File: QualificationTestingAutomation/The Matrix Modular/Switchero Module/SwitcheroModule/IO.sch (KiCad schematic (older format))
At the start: 8 parts, among them J1 Conn_02x32_Counter_Clockwise_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, J2 OBD Connector, J3 OBD Connector, J6 Conn_02x32_Counter_Clockwise_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

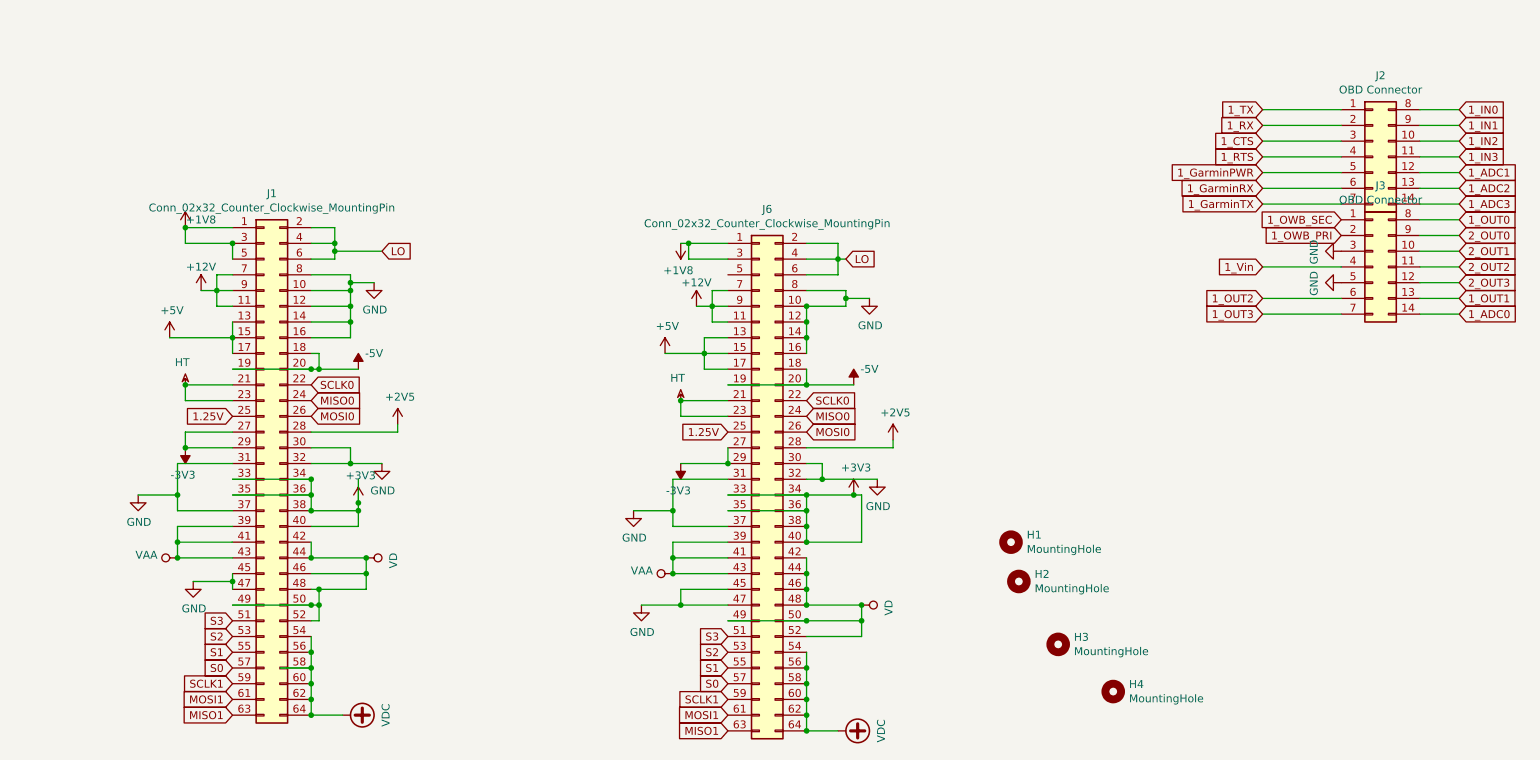
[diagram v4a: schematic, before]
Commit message: IO clean up added the 1v25 reference to Matrix Changed Some of the labels to more legible names.
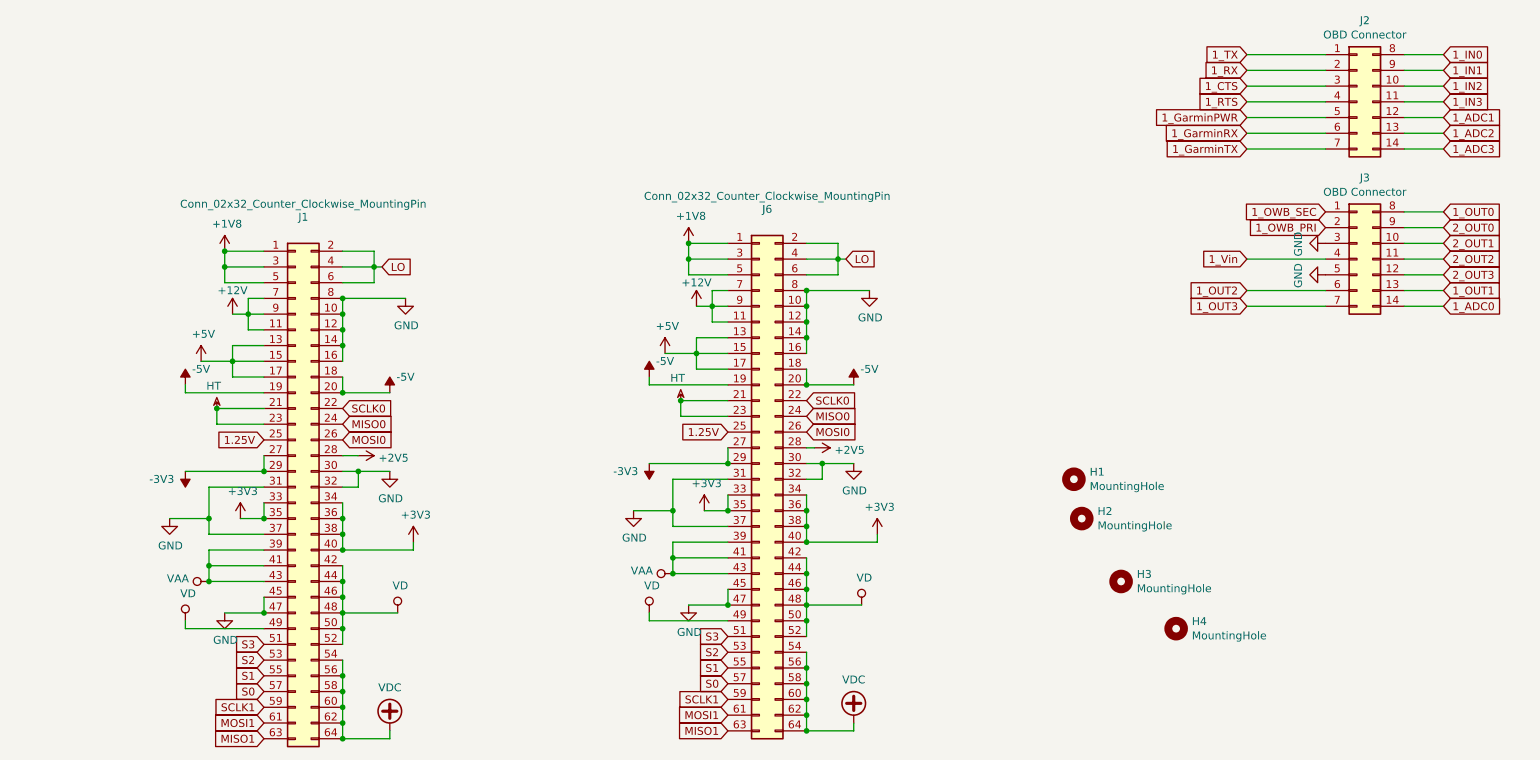
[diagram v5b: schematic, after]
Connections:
- net +1V8: now also J6.5 (Pin_5)
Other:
- moved on the sheet: H2, H3, H4, J2, J3

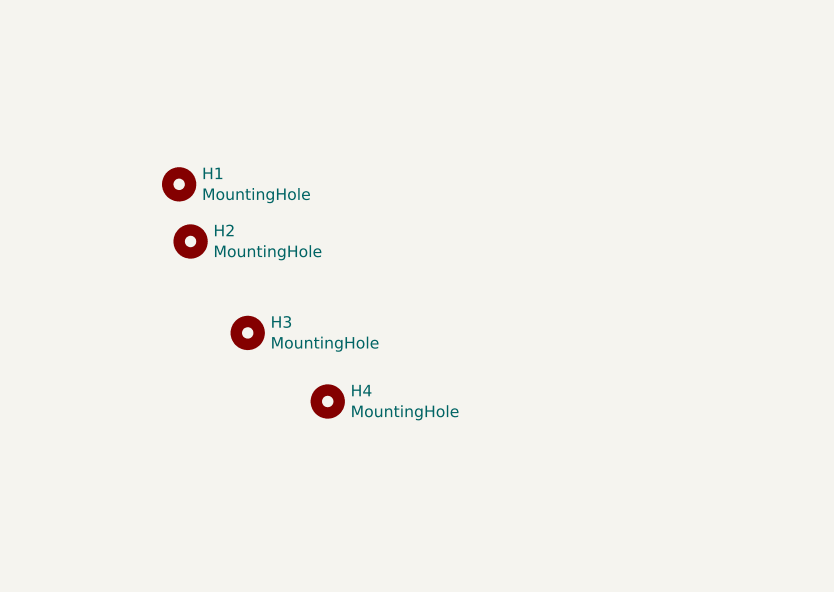
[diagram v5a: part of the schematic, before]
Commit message: Reefero Module PCB design
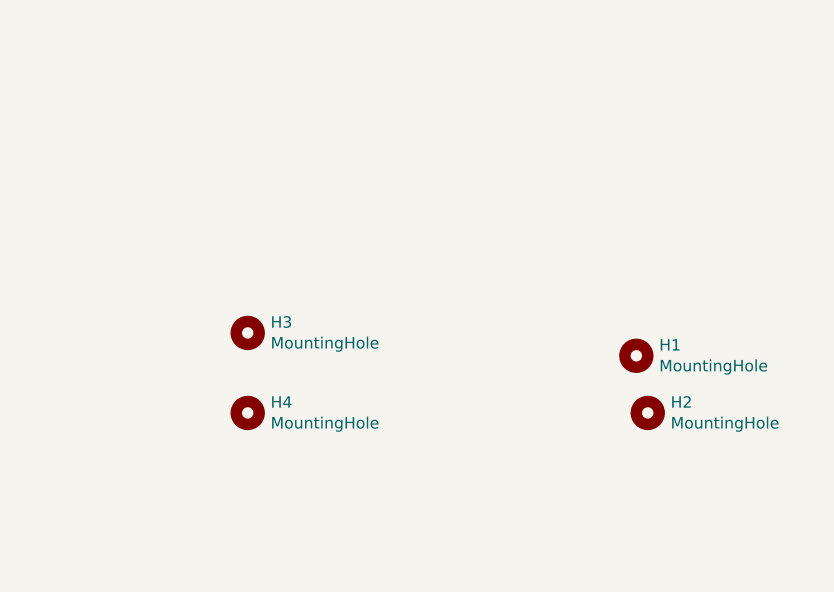
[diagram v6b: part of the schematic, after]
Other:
- moved on the sheet: H1, H2, H4
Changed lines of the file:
@@
 L Mechanical:MountingHole H?
 U 1 1 5CA6BACD
-P 8100 3700
+P 10100 4450
 AR Path="/5D942532/5CA6BACD" Ref="H?"  Part="1"
 AR Path="/5D968A33/5CA6BACD" Ref="H?"  Part="1"
 AR Path="/5C90F517/5CA6BACD" Ref="H1"  Part="1"
-F 0 "H1" H 8200 3746 50  0000 L CNN
-F 1 "MountingHole" H 8200 3655 50  0000 L CNN
-F 2 "MountingHole:MountingHole_2.5mm" H 8100 3700 50  0001 C CNN
-F 3 "~" H 8100 3700 50  0001 C CNN
-	1    8100 3700
+F 0 "H1" H 10200 4496 50  0000 L CNN
+F 1 "MountingHole" H 10200 4405 50  0000 L CNN
+F 2 "MountingHole:MountingHole_2.5mm" H 10100 4450 50  0001 C CNN
+F 3 "~" H 10100 4450 50  0001 C CNN
+	1    10100 4450
 	1    0    0    -1
 $EndComp
@@
 L Mechanical:MountingHole H?
 U 1 1 5E817FBB
-P 8150 3950
+P 10150 4700
 AR Path="/5D942532/5E817FBB" Ref="H?"  Part="1"
 AR Path="/5D968A33/5E817FBB" Ref="H?"  Part="1"
 AR Path="/5C90F517/5E817FBB" Ref="H2"  Part="1"
-F 0 "H2" H 8250 3996 50  0000 L CNN
-F 1 "MountingHole" H 8250 3905 50  0000 L CNN
-F 2 "MountingHole:MountingHole_2.5mm" H 8150 3950 50  0001 C CNN
-F 3 "~" H 8150 3950 50  0001 C CNN
-	1    8150 3950
+F 0 "H2" H 10250 4746 50  0000 L CNN
+F 1 "MountingHole" H 10250 4655 50  0000 L CNN
+F 2 "MountingHole:MountingHole_2.5mm" H 10150 4700 50  0001 C CNN
+F 3 "~" H 10150 4700 50  0001 C CNN
+	1    10150 4700
 	1    0    0    -1
 $EndComp
@@
 L Mechanical:MountingHole H?
 U 1 1 5E82AE9C
-P 8750 4650
+P 8400 4700
 AR Path="/5D942532/5E82AE9C" Ref="H?"  Part="1"
 AR Path="/5D968A33/5E82AE9C" Ref="H?"  Part="1"
 AR Path="/5C90F517/5E82AE9C" Ref="H4"  Part="1"
-F 0 "H4" H 8850 4696 50  0000 L CNN
-F 1 "MountingHole" H 8850 4605 50  0000 L CNN
-F 2 "MountingHole:MountingHole_2.5mm" H 8750 4650 50  0001 C CNN
-F 3 "~" H 8750 4650 50  0001 C CNN
-	1    8750 4650
+F 0 "H4" H 8500 4746 50  0000 L CNN
+F 1 "MountingHole" H 8500 4655 50  0000 L CNN
+F 2 "MountingHole:MountingHole_2.5mm" H 8400 4700 50  0001 C CNN
+F 3 "~" H 8400 4700 50  0001 C CNN
+	1    8400 4700
 	1    0    0    -1
 $EndComp
